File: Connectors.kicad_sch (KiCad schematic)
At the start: 12 parts, among them J1 430450212, J14 ET60S-D04-3-08-D04-X-R1-S, J18 430450212, J19 DF11-10DS-2DSA05, J2 IPS1-105-01-L-D, J3 IPS1-105-01-L-D, J4 Conn_01x04_Pin, J6 Conn_01x02_Pin, J8 430450612, U1 282837-6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

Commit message: Work done on 12/16/2024
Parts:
- removed J4: Conn_01x04_Pin, Connector_PinHeader_2.54mm:PinHeader_1x04_P2.54mm_Vertical, symbol Connector:Conn_01x04_Pin
- added J4: Conn_01x07_Pin, Connector_PinHeader_2.54mm:PinHeader_1x07_P2.54mm_Vertical, symbol Connector:Conn_01x07_Pin
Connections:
- net GPIO1: now also J4.1 (Pin_1)
- net GPIO2: now also J4.2 (Pin_2)
- net GPIO3: now also J4.3 (Pin_3)
- net GPIO4: now also J4.4 (Pin_4)
- net GPIO5: now also J4.5 (Pin_5)
- net GPIO6: now also J4.6 (Pin_6)
- net GPIO7: now also J4.7 (Pin_7)
- net CS: no longer names the net of J19.20
- net MISO: no longer names the net of J19.17
- net MOSI: no longer names the net of J19.18
- net SCLK: no longer names the net of J19.19
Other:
- note removed: "SPI Test Point"

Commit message: Work done on 12/16/2024 v2
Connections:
- net A+: now also J14.02, J19.17; no longer J14.01
- net A-: now also J14.01, J19.18; no longer J14.02
- no-connect marks 25 -> 27

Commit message: Work done on 12/17/2024
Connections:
- net A+: no longer J14.02, J19.4
- net A-: no longer J14.01, J19.6
- net GPIO1: now also J4.7 (Pin_7); no longer J4.1 (Pin_1)
- net GPIO2: now also J4.6 (Pin_6); no longer J4.2 (Pin_2)
- net GPIO3: now also J4.5 (Pin_5); no longer J4.3 (Pin_3)
- net GPIO5: now also J4.3 (Pin_3); no longer J4.5 (Pin_5)
- net GPIO6: now also J4.2 (Pin_2); no longer J4.6 (Pin_6)
- net GPIO7: now also J4.1 (Pin_1); no longer J4.7 (Pin_7)
- new net Aout+: J14.02, J19.4
- new net Aout-: J14.01, J19.6

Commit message: Work done on 12/17/2024 final
Am i done??????
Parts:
- added J10, J5: Conn_01x01_Pin, Connector_PinHeader_2.54mm:PinHeader_1x01_P2.54mm_Vertical, symbol Connector:Conn_01x01_Pin
- added U4: 282837-3, 282837_3footprints:282837-3_TYC, symbol 2024-10-03_00-20-30:282837-3
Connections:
- net P06 is gone; now on net P05: J14.P06_1 (P06)
- net P08 is gone; now on net P07: J14.P08_1 (P08), J2.02, J2.03, J3.02, J3.03, U2.8 (GND), U3.1
- net P05: now also U4.3
- net P07: now also U4.2
- net PWMC0: now also J10.1 (Pin_1)
- new net PWMC0_OUT: J5.1 (Pin_1), U4.1
- no-connect marks 27 -> 25
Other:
- note added: "BACKUP SERVO CONNECTIONS"

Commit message: board review 12/30 midway
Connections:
- net 48V_GND: now also J14.16; no longer J14.23
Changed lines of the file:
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@@
+	)
+	(no_connect
+		(at 217.17 72.39)
+	)
+	(no_connect
+		(at 31.75 38.1)
+	)
+	(no_connect
+		(at 31.75 40.64)
+	)
+	(no_connect
+		(at 217.17 80.01)
+	)
+	(no_connect
+		(at 217.17 59.69)
+	)
+	(no_connect
+		(at 217.17 82.55)
+	)
+	(no_connect
+		(at 242.57 49.53)
 	)
 	(no_connect
@@
 	)
 	(no_connect
-		(at 217.17 72.39)
-	)
-	(no_connect
-		(at 31.75 38.1)
-	)
-	(no_connect
-		(at 31.75 40.64)
-	)
-	(no_connect
-		(at 217.17 80.01)
-	)
-	(no_connect
-		(at 217.17 59.69)
-	)
-	(no_connect
-		(at 217.17 82.55)
-	)
-	(no_connect
-		(at 242.57 49.53)
-	)
-	(no_connect
 		(at 217.17 87.63)
-	)
-	(no_connect
-		(at 217.17 90.17)
 	)
 	(no_connect
@@
 	(no_connect
 		(at 217.17 39.37)
+	)
+	(no_connect
+		(at 242.57 64.77)
 	)
 	(no_connect
@@
 		)
 	)
+	(global_label "48V"
+		(shape input)
+		(at 242.57 59.69 0)
+		(fields_autoplaced yes)
+		(effects
+			(font
+				(size 0.762 0.762)
+			)
+			(justify left)
+		)
+		(property "Intersheetrefs" "${INTERSHEET_REFS}"
+			(at 246.4659 59.69 0)
+			(effects
+				(font
+					(size 1.27 1.27)
+				)
+				(justify left)
+				(hide yes)
+			)
+		)
+	)
 	(global_label "A-"
 		(shape input)
@@
 		)
 	)
+	(global_label "48V_GND"
+		(shape input)
+		(at 217.17 90.17 180)
+		(fields_autoplaced yes)
+		(effects
+			(font
+				(size 0.762 0.762)
+			)
+			(justify right)
+		)
+		(property "Intersheetrefs" "${INTERSHEET_REFS}"
+			(at 210.3712 90.17 0)
+			(effects
+				(font
+					(size 1.27 1.27)
+				)
+				(justify right)
+				(hide yes)
+			)
+		)
+	)
 	(global_label "12V_GND"
 		(shape input)
@@
 		)
 	)
-	(global_label "48V_GND"
-		(shape input)
-		(at 242.57 64.77 0)
-		(fields_autoplaced yes)
-		(effects
-			(font
-				(size 0.762 0.762)
-			)
-			(justify left)
-		)
-		(property "Intersheetrefs" "${INTERSHEET_REFS}"
-			(at 249.3688 64.77 0)
-			(effects
-				(font
-					(size 1.27 1.27)
-				)
-				(justify left)
-				(hide yes)
-			)
-		)
-	)
 	(global_label "Aout-"
 		(shape input)
@@
 				(hide yes)
 			)
-		)
-	)
-	(global_label "48V"
-		(shape input)
-		(at 242.57 59.69 0)
-		(fields_autoplaced yes)
-		(effects
-			(font
-				(size 0.762 0.762)
-			)
-			(justify left)
-		)
-		(property "Intersheetrefs" "${INTERSHEET_REFS}"
-			(at 246.4659 59.69 0)
-			(effects
-				(font
-					(size 1.27 1.27)
-				)
-				(justify left)
-				(hide yes)
-			)

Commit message: changes 1/3/25
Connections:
- net 48V: now also J14.13, J14.14
- net 5V_GND: now also J14.12, J2.02, J3.02
- net P07: no longer J2.02, J3.02
- net Telemetry: now also J2.05, J3.05; no longer J2.09, J3.09
- no-connect marks 25 -> 22

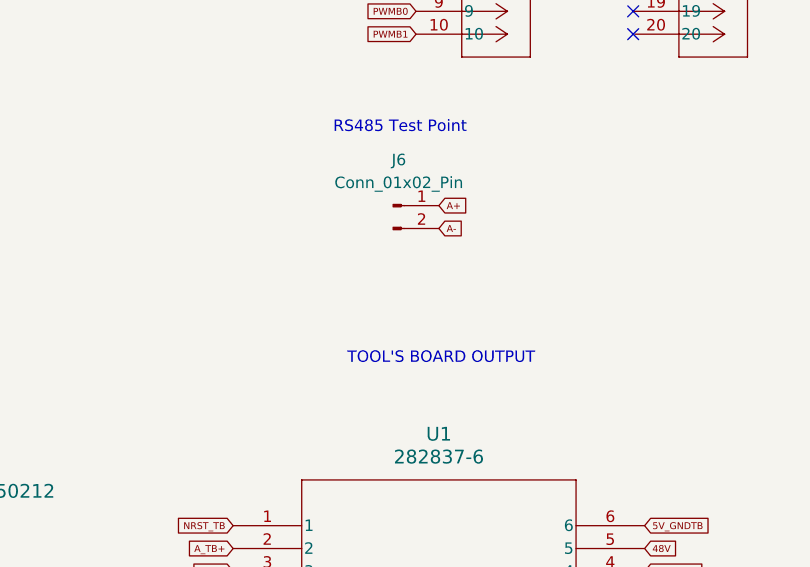
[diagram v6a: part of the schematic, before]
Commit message: correct solenoid connector + some silkscreen additions
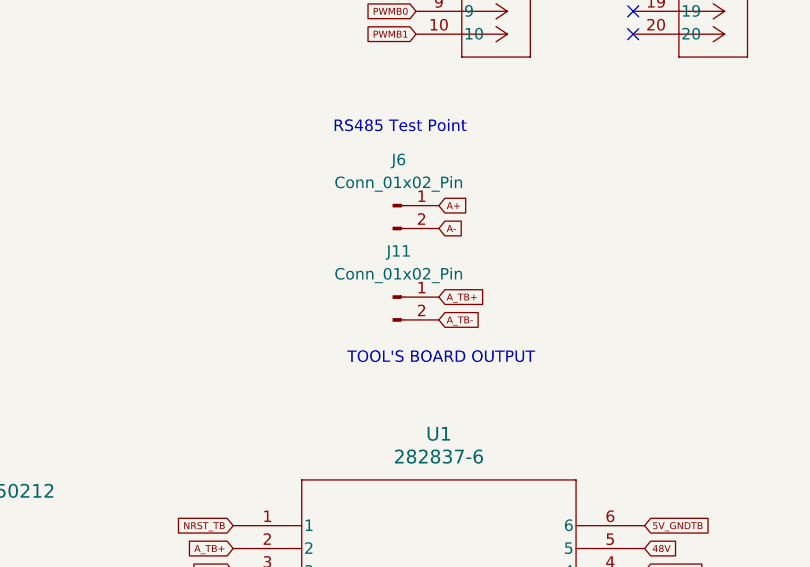
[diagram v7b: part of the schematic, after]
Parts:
- added J11: Conn_01x02_Pin, Connector_PinHeader_2.54mm:PinHeader_1x02_P2.54mm_Vertical, symbol Connector:Conn_01x02_Pin
- U3: footprint Connector_PinHeader_2.54mm:PinHeader_1x08_P2.54mm_Vertical -> 1778612:PHOENIX_1778612
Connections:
- net A_TB+: now also J11.1 (Pin_1)
- net A_TB-: now also J11.2 (Pin_2)
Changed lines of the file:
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@@
+		)
+	)
+	(global_label "A_TB-"
+		(shape input)
+		(at 128.27 86.36 0)
+		(fields_autoplaced yes)
+		(effects
+			(font
+				(size 0.762 0.762)
+			)
+			(justify left)
+		)
+		(property "Intersheetrefs" "${INTERSHEET_REFS}"
+			(at 133.5811 86.36 0)
+			(effects
+				(font
+					(size 1.27 1.27)
+				)
+				(justify left)
+				(hide yes)
+			)
 		)
 	)
@@
 		(property "Intersheetrefs" "${INTERSHEET_REFS}"
 			(at 62.9329 58.42 0)
+			(effects
+				(font
+					(size 1.27 1.27)
+				)
+				(justify left)
+				(hide yes)
+			)
+		)
+	)
+	(global_label "A_TB+"
+		(shape input)
+		(at 128.27 83.82 0)
+		(fields_autoplaced yes)
+		(effects
+			(font
+				(size 0.762 0.762)
+			)
+			(justify left)
+		)
+		(property "Intersheetrefs" "${INTERSHEET_REFS}"
+			(at 133.5811 83.82 0)
 			(effects
 				(font
@@
 			)
 		)
-		(property "Footprint" "Connector_PinHeader_2.54mm:PinHeader_1x08_P2.54mm_Vertical"
+		(property "Footprint" "1778612:PHOENIX_1778612"
 			(at 104.14 152.4 0)
 			(effects
@@
 					(unit 1)
 				)
+			)
+		)
+	)
+	(symbol
+		(lib_id "Connector:Conn_01x02_Pin")
+		(at 123.19 83.82 0)
+		(unit 1)
+		(exclude_from_sim no)
+		(in_bom yes)
+		(on_board yes)
+		(dnp no)
+		(fields_autoplaced yes)
+		(property "Reference" "J11"
+			(at 123.825 78.74 0)
+			(effects
+				(font
+					(size 1.27 1.27)
+				)
+			)
+		)
+		(property "Value" "Conn_01x02_Pin"
+			(at 123.825 81.28 0)
+			(effects
+				(font
+					(size 1.27 1.27)
+				)
+			)
+		)
+		(property "Footprint" "Connector_PinHeader_2.54mm:PinHeader_1x02_P2.54mm_Vertical"
+			(at 123.19 83.82 0)
+			(effects
+				(font
+					(size 1.27 1.27)
+				)
+				(hide yes)
+			)
+		)
+		(property "Datasheet" "~"
+			(at 123.19 83.82 0)
+			(effects
+				(font
+					(size 1.27 1.27)
+				)
+				(hide yes)
+			)
+		)
+		(property "Description" "Generic connector, single row, 01x02, script generated"
+			(at 123.19 83.82 0)
+			(effects
+				(font
+					(size 1.27 1.27)
+				)
+				(hide yes)
+			)
+		)
+		(pin "1"
+		)
+		(pin "2"
+		)
+		(instances
+			(project "X17_Backplane"
+				(path "/0b609d63-053d-4947-8bc2-b53c83cfcb53/ad869c69-8d32-4ec0-b8bb-9dda93ac11ca"
+					(reference "J11")
+					(unit 1)
+				)

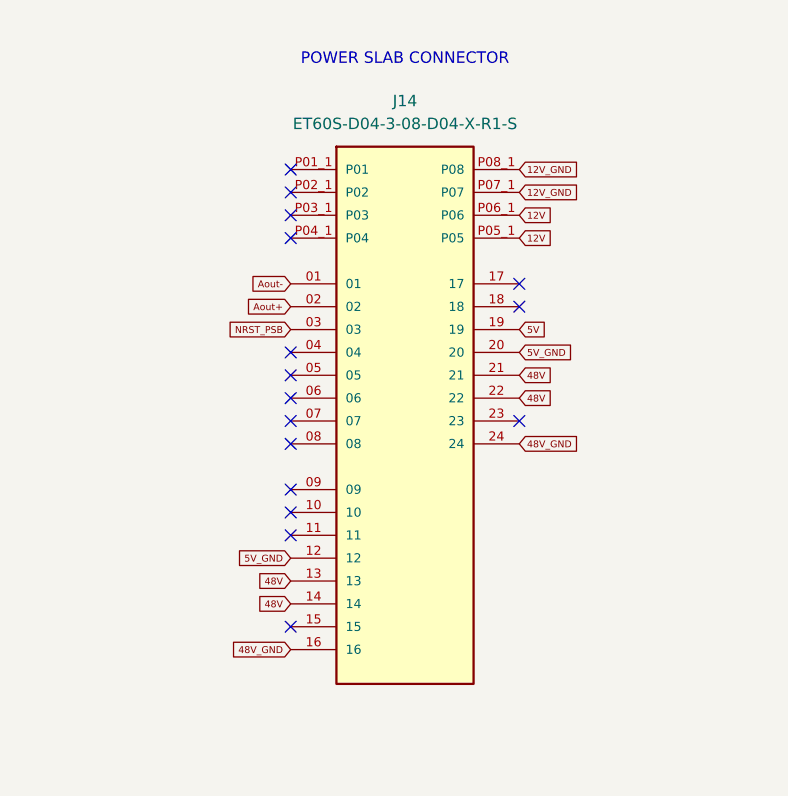
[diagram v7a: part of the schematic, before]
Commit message: some pinout changes
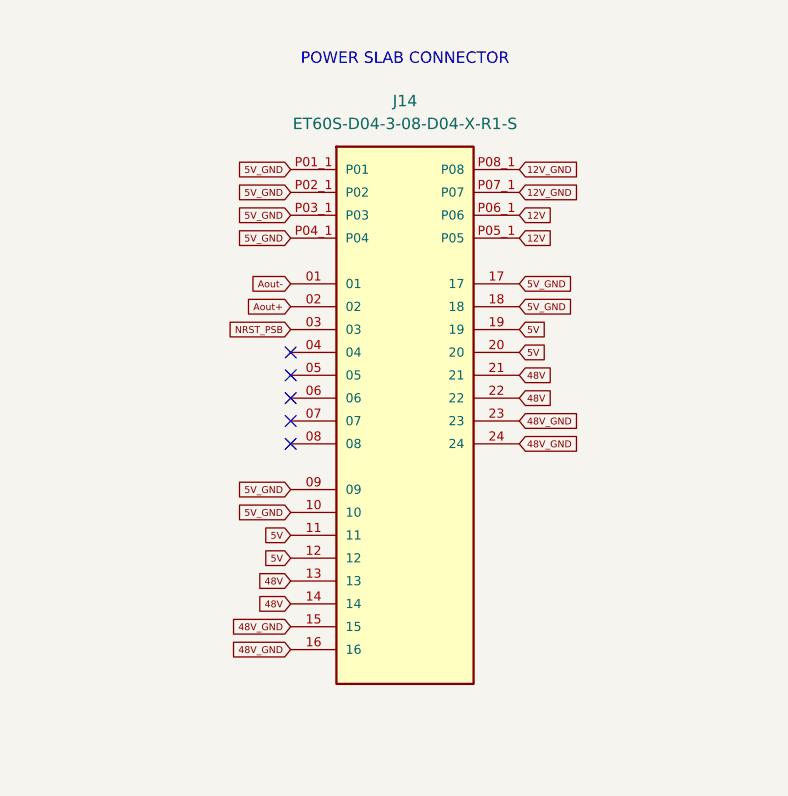
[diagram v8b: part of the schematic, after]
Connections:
- net P02 is gone; now on net P01: J14.P02_1 (P02)
- net P03 is gone; now on net P01: J14.P03_1 (P03)
- net P04 is gone; now on net P01: J14.P04_1 (P04)
- net 48V_GND: now also J14.15, J14.23
- net 5V: now also J14.11, J14.12, J14.20
- net P01: now also J14.09, J14.10, J14.17, J14.18, J19.2, J2.02, J3.02, J8.2
- removed net 5V_GND: J14.12, J14.20, J19.2, J2.02, J3.02, J8.2
- no-connect marks 22 -> 11
